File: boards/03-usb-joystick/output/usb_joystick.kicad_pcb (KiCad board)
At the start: 2 copper layers, 80 x 60 mm, 19 parts, among them J1 USB-C, J2 Joystick, SW1 Button, SW2 Button, SW3 Button, SW4 Button, U1 MCU, Y1 16MHz

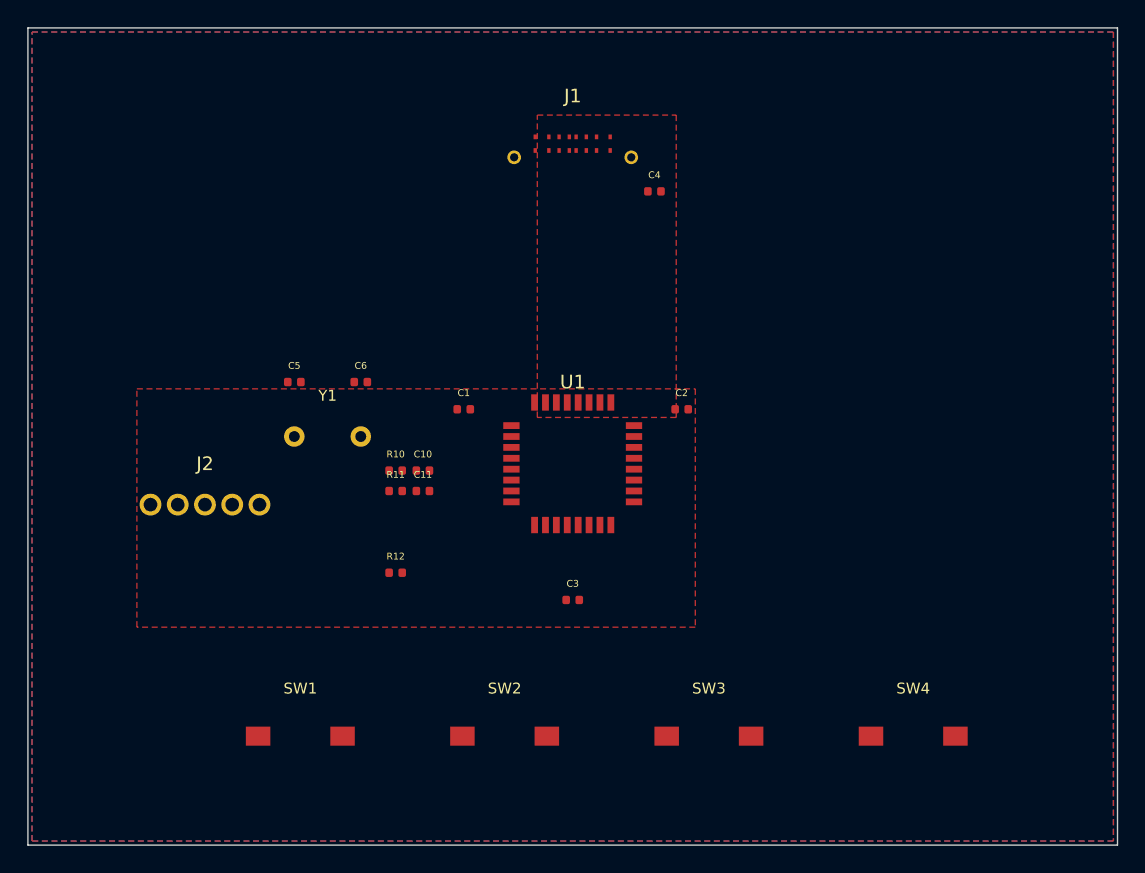
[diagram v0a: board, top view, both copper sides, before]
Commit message: feat(optim): rotate edge-constrained connectors to face off-board (#4525)
* feat(optim): rotate edge-constrained connectors to face off-board

An `EdgeConstraint` could only translate a component toward its board
edge. A USB-C receptacle could therefore sit flush at the perimeter with
its plug opening aimed at the board interior -- placement the
EDGE_CONNECTOR_PLACEMENT check accepts but no cable can mate with. That
is exactly how board-03's J1 shipped: 7.6 mm inboard of the north edge,
mouth pointing at the buttons.

Library capability:

- `EdgeConstraint.mating_face_offset_deg` -- the off-board direction of a
  footprint's mating face in its own 0-degree frame (KiCad board frame,
  +Y = south). `None` keeps the pre-existing translation-only behavior.
- `compute_edge_orientation_torque()` -- torsion spring toward alignment
  with the assigned edge's outward `Edge.normal()`, summed into
  `PlacementOptimizer.compute_forces_and_torques()` alongside the
  existing 90-degree rotation-potential torque. Its magnitude saturates
  past 90 degrees of misalignment so the 180-degree (mouth-inward) case
  is not a zero-torque saddle.
- `edge_orientation_potential_energy()` -- added to `compute_energy()`,
  without which `run()` calls convergence (it samples linear velocity
  only) while a connector is still mid-flip.
- `snap_rotations()` resolves a hinted edge connector to the grid slot
  that faces off-board instead of the nearest one; the board boundary's
  own alignment torque has equal wells 180 degrees apart, so the discrete
  step is where the requirement has to be settled deterministically.
- `detect_edge_components(mating_faces=...)` / `from_pcb(mating_faces=...)`
  thread caller-supplied per-reference hints through.

board-03 consumes it:

- J1 rotated 180 degrees so the plug opening faces off the north edge,
  seated 0.5 mm inside Edge.Cuts, and given F.CrtYd artwork covering the
  real receptacle body -- without it the footprint claims to be only its
  pad field and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
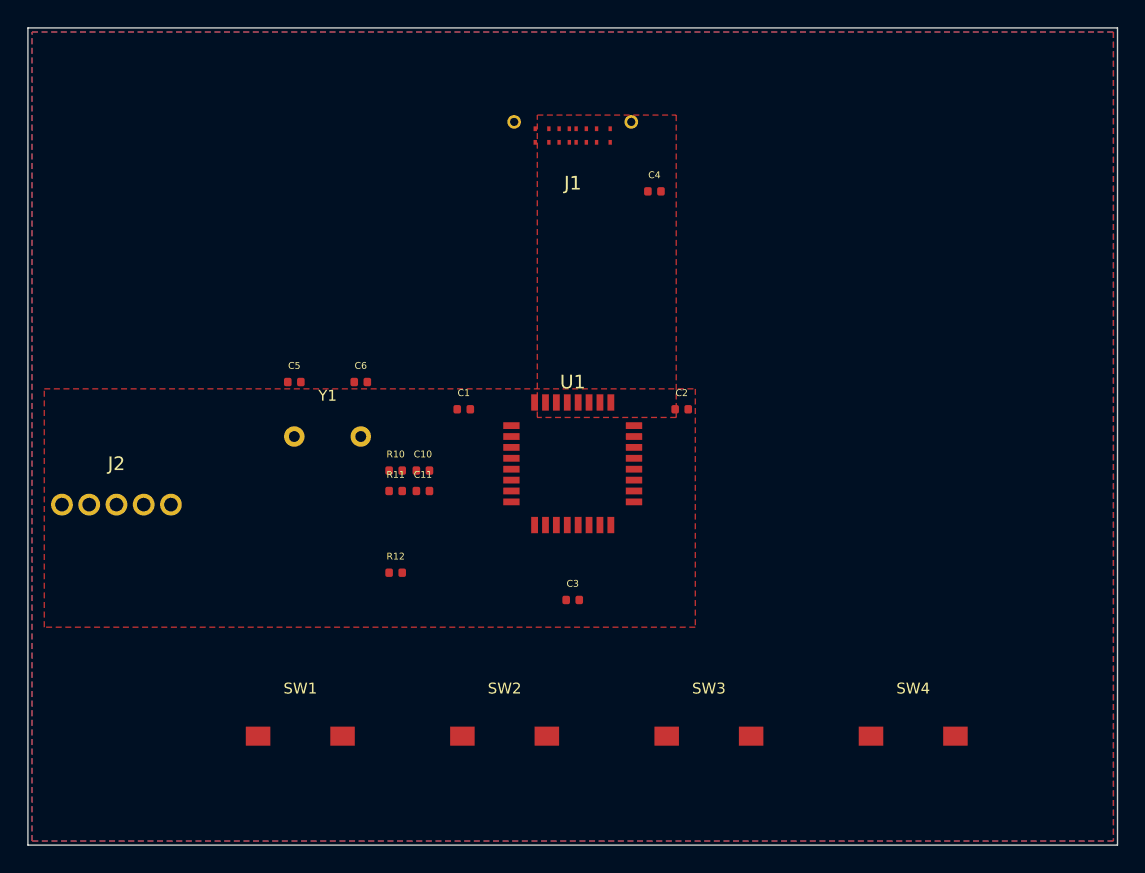
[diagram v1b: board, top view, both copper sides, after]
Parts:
- moved J2 6.50 mm to (115.0, 92.5)
- moved J1 0.40 mm to (148.5, 65.9), turned to 180 degrees
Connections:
- U1 pad 27: USB_CC2 -> USB_CC1
- U1 pad 28: USB_D- -> USB_D+
- U1 pad 29: USB_D+ -> USB_D-
- U1 pad 30: USB_CC1 -> USB_CC2
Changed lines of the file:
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@@
     (pad "25" smd rect (at 2.800 -4.500) (size 0.5 1.2) (layers "F.Cu" "F.Paste" "F.Mask") (net 3 "GND"))
     (pad "26" smd rect (at 2.000 -4.500) (size 0.5 1.2) (layers "F.Cu" "F.Paste" "F.Mask") (net 1 "VBUS"))
-    (pad "27" smd rect (at 1.200 -4.500) (size 0.5 1.2) (layers "F.Cu" "F.Paste" "F.Mask") (net 7 "USB_CC2"))
-    (pad "28" smd rect (at 0.400 -4.500) (size 0.5 1.2) (layers "F.Cu" "F.Paste" "F.Mask") (net 5 "USB_D-"))
-    (pad "29" smd rect (at -0.400 -4.500) (size 0.5 1.2) (layers "F.Cu" "F.Paste" "F.Mask") (net 4 "USB_D+"))
-    (pad "30" smd rect (at -1.200 -4.500) (size 0.5 1.2) (layers "F.Cu" "F.Paste" "F.Mask") (net 6 "USB_CC1"))
+    (pad "27" smd rect (at 1.200 -4.500) (size 0.5 1.2) (layers "F.Cu" "F.Paste" "F.Mask") (net 6 "USB_CC1"))
+    (pad "28" smd rect (at 0.400 -4.500) (size 0.5 1.2) (layers "F.Cu" "F.Paste" "F.Mask") (net 4 "USB_D+"))
+    (pad "29" smd rect (at -0.400 -4.500) (size 0.5 1.2) (layers "F.Cu" "F.Paste" "F.Mask") (net 5 "USB_D-"))
+    (pad "30" smd rect (at -1.200 -4.500) (size 0.5 1.2) (layers "F.Cu" "F.Paste" "F.Mask") (net 7 "USB_CC2"))
     (pad "31" smd rect (at -2.000 -4.500) (size 0.5 1.2) (layers "F.Cu" "F.Paste" "F.Mask") (net 3 "GND"))
     (pad "32" smd rect (at -2.800 -4.500) (size 0.5 1.2) (layers "F.Cu" "F.Paste" "F.Mask") (net 3 "GND"))
@@
   (footprint "Connector_USB:USB_C_Receptacle_GCT_USB4105"
     (layer "F.Cu")
-    (at 148.5 65.5)
+    (at 148.5 65.9 180)
     (attr smd)
     (locked yes)
@@
     (fp_text value "USB-C" (at 0 4) (layer "F.Fab")
       (effects (font (size 1 1) (thickness 0.15)))
+    )
+    (fp_rect (start -5.32 -1.05) (end 5.32 7.9)
+      (stroke (width 0.05) (type solid)) (fill no) (layer "F.CrtYd")
     )
     (pad "A1" smd rect (at -2.75 0.00) (size 0.25 0.35) (layers "F.Cu" "F.Paste" "F.Mask") (net 3 "GND"))
@@
   (footprint "Module:Joystick_Analog"
     (layer "F.Cu")
-    (at 121.5 92.5)
+    (at 115.0 92.5)
     (attr through_hole)
     (locked yes)
@@
   (footprint "Resistor_SMD:R_0402_1005Metric"
     (layer "F.Cu")
-    (at 135.5 90)
+    (at 135.5 90.0)
     (fp_text reference "R10" (at 0 -1.2) (layer "F.SilkS")
       (effects (font (size 0.5 0.5) (thickness 0.1)))
@@
   (footprint "Capacitor_SMD:C_0402_1005Metric"
     (layer "F.Cu")
-    (at 137.5 90)
+    (at 137.5 90.0)
     (fp_text reference "C10" (at 0 -1.2) (layer "F.SilkS")
       (effects (font (size 0.5 0.5) (thickness 0.1)))
@@
   		)
   		(rotate
-  			(xyz 0 0 0)
+  			(xyz 0 0 90)
   		)
   	)
@@
   		)
   		(rotate
-  			(xyz 0 0 0)
+  			(xyz 0 0 90)
   		)
   	)
@@
   		)
   		(rotate
-  			(xyz 0 0 0)
+  			(xyz 0 0 90)
   		)
   	)
@@
   		)
   		(rotate
-  			(xyz 0 0 0)
+  			(xyz 0 0 90)
   		)
   	)
@@
     (fill yes (thermal_gap 0.3) (thermal_bridge_width 0.4)
     )
-    (polygon (pts (xy 116.5 84) (xy 157.5 84) (xy 157.5 101.5) (xy 116.5 101.5))
-    )
-  )
+    (polygon (pts (xy 109.7 84.0) (xy 157.5 84.0) (xy 157.5 101.5) (xy 109.7 101.5))
+    )
+  )
